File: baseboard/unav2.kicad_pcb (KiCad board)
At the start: 2 copper layers, 39 parts, among them IC1 MPM36xx, P1 SWD_TC, SW1 KEY_UP, SW2 KEY1, SW3 KEY0, SW4 Reset, U1 STM32F405RGTx, U2 AP2121AK-3.3

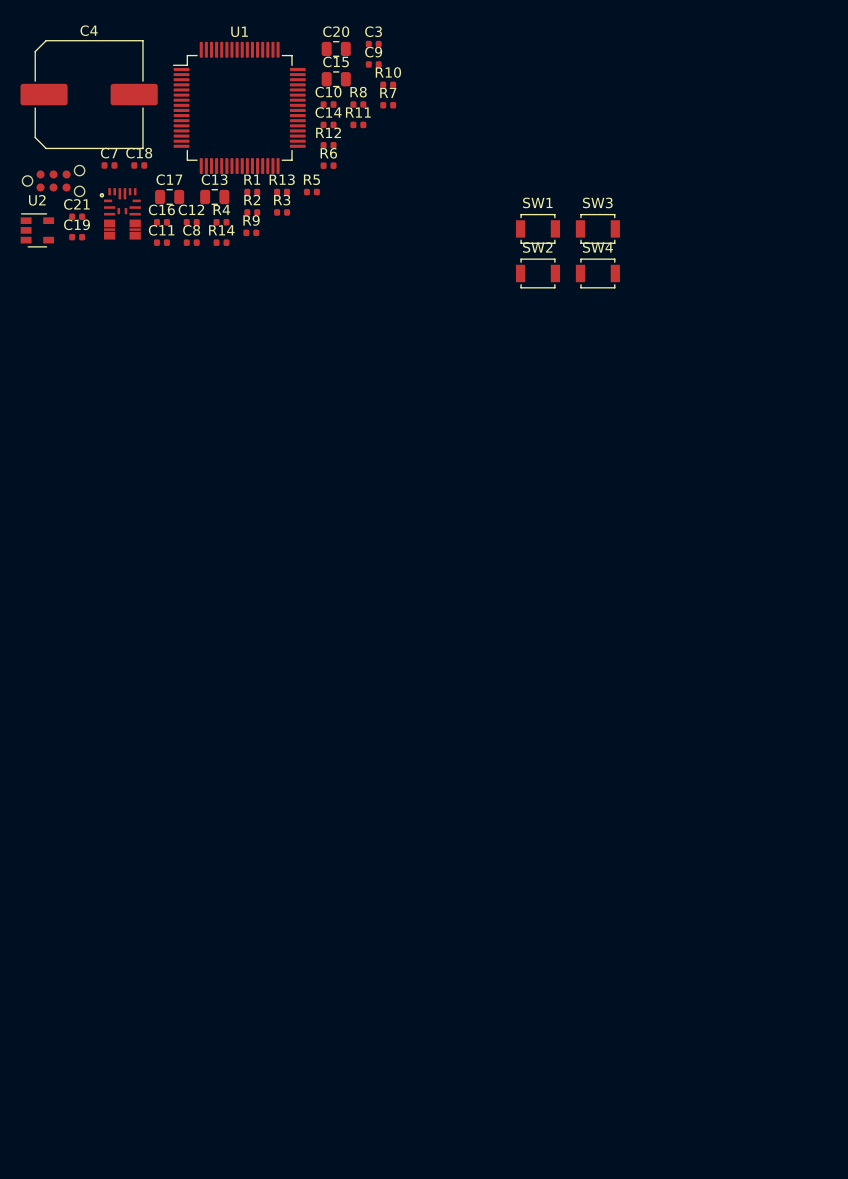
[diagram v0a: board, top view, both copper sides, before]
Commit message: test design of mcu+driver boards(do not build!! it is just less than an idea right now)
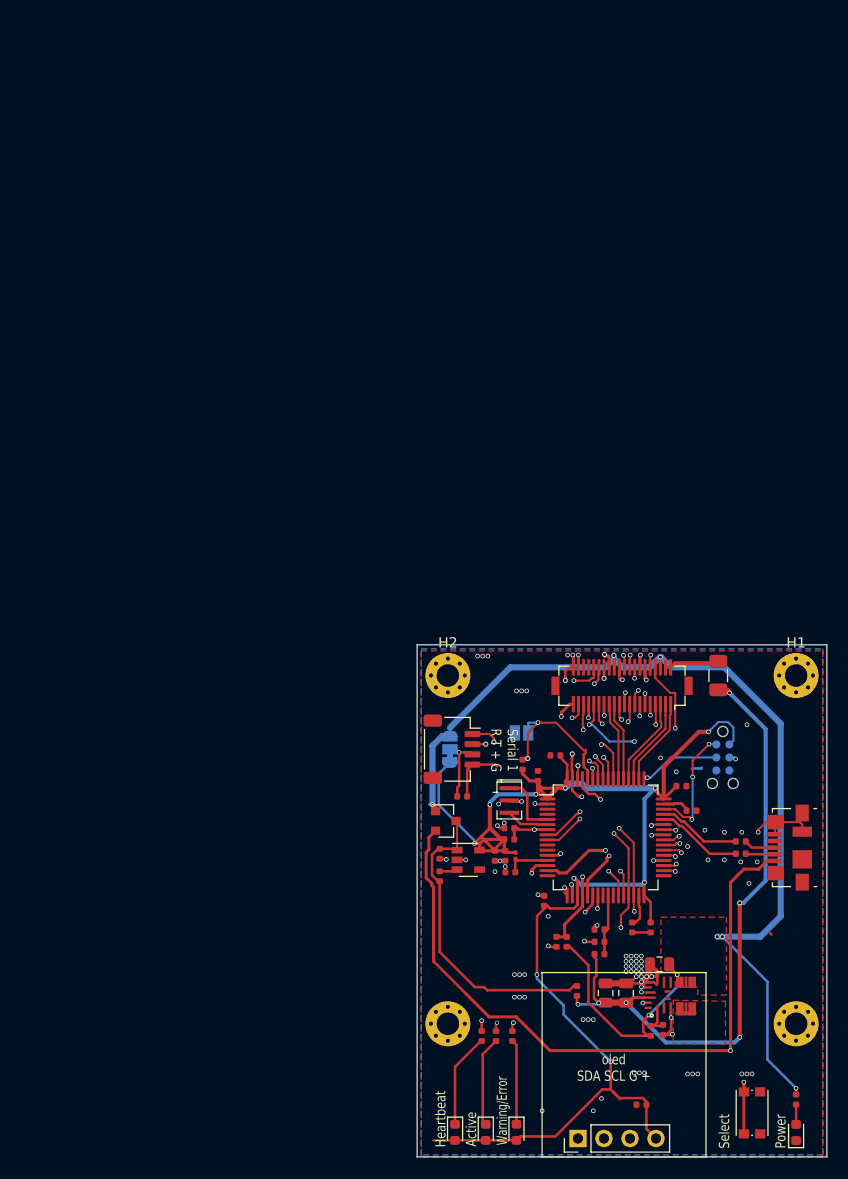
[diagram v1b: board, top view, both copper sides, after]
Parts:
- removed C20: 4.7uF, Capacitor_SMD:C_0805_2012Metric
- removed R11, R13: 10k, Resistor_SMD:R_0402_1005Metric
- removed R12, R8: 330, Resistor_SMD:R_0402_1005Metric
- removed R9: 22, Resistor_SMD:R_0402_1005Metric
- removed SW2: KEY1, Button_Switch_SMD:SW_SPST_B3U-1000P
- removed SW3: KEY0, Button_Switch_SMD:SW_SPST_B3U-1000P
- removed SW4: Reset, Button_Switch_SMD:SW_SPST_B3U-1000P
- added C22: C, Capacitor_SMD:C_0402_1005Metric, F.Cu at (154.4, 64.8)
- added C5: 100nF, Capacitor_SMD:C_0402_1005Metric, F.Cu at (167.8, 77.8)
- added C6: C, Capacitor_SMD:C_0402_1005Metric, F.Cu at (171.9, 94.9)
- added D1: White, LED_SMD:LED_0603_1608Metric, F.Cu at (187.0, 97.6)
- added D2: BAT54C, Package_TO_SOT_SMD:SOT-23, F.Cu at (152.8, 67.2)
- added D3: Blue, LED_SMD:LED_0603_1608Metric, F.Cu at (153.7, 97.6)
- added D4: Yellow, LED_SMD:LED_0603_1608Metric, F.Cu at (156.7, 97.6)
- added D5: Red, LED_SMD:LED_0603_1608Metric, F.Cu at (159.7, 97.6)
- added F1: Polyfuse_Small, Fuse:Fuse_1206_3216Metric, F.Cu at (179.4, 53.0)
- added H1: MountingHole, MountingHole:MountingHole_2.2mm_M2_Pad_Via, F.Cu at (187.0, 53.0)
- added H2: MountingHole, MountingHole:MountingHole_2.2mm_M2_Pad_Via, F.Cu at (153.0, 53.0)
- added H3: MountingHole, MountingHole:MountingHole_2.2mm_M2_Pad_Via, F.Cu at (153.0, 87.0)
- added H4: MountingHole, MountingHole:MountingHole_2.2mm_M2_Pad_Via, F.Cu at (187.0, 87.0)
- added J1: Conn_02x20_Top_Bottom, agg-kicad:Hirose_DF12_DF12B-40DS-0.5V(86), F.Cu at (170.0, 54.0)
- added J4: SERIAL1, Connector_JST:JST_SH_SM04B-SRSS-TB_1x04-1MP_P1.00mm_Horizontal, F.Cu at (153.4, 60.2)
- added J5: OLED, Connector_PinHeader_2.54mm:PinHeader_1x04_P2.54mm_Vertical, F.Cu at (165.7, 98.2)
- added J6: USB_B_Micro, Connector_USB:USB_Micro-B_Molex_47346-0001, F.Cu at (186.4, 69.8)
- added JP1: BOOT, Jumper:SolderJumper-2_P1.3mm_Open_Pad1.0x1.5mm, B.Cu at (160.2, 58.6)
- added JP3: S1_VSEL, Jumper:SolderJumper-3_P1.3mm_Bridged12_RoundedPad1.0x1.5mm, B.Cu at (153.2, 60.2)
- added L1: L_Small, Inductor_SMD:L_0201_0603Metric, F.Cu at (159.6, 70.6)
- added R15: 1k, Resistor_SMD:R_0402_1005Metric, F.Cu at (167.8, 79.0)
- added R16: 1k, Resistor_SMD:R_0402_1005Metric, F.Cu at (187.0, 94.4)
- added R17: 330, Resistor_SMD:R_0402_1005Metric, F.Cu at (156.3, 88.2)
- added R18: 330, Resistor_SMD:R_0402_1005Metric, F.Cu at (157.7, 88.2)
- added R19: 330, Resistor_SMD:R_0402_1005Metric, F.Cu at (159.3, 88.2)
- added Y1: 8MHz, Crystal:Resonator_SMD_muRata_CSTxExxV-3Pin_3.0x1.1mm, F.Cu at (159.0, 65.2)
- added e: 22, Resistor_SMD:R_0402_1005Metric, F.Cu at (181.6, 69.2)
- C13: value 4.7uf -> 1uF; footprint Capacitor_SMD:C_0805_2012Metric -> Capacitor_SMD:C_0402_1005Metric
- C18: value 10nF -> 100nF
- C19: value 10nF -> 4.7uf; footprint Capacitor_SMD:C_0402_1005Metric -> Capacitor_SMD:C_0805_2012Metric
- C4: value SUPERCAP -> 100nF; footprint Capacitor_SMD:C_Elec_10x10.2 -> Capacitor_SMD:C_0402_1005Metric
- IC1: footprint agg:QFN-20-MPS-3x5x1.6mm -> agg-kicad:QFN-20-MPS-3x5x1.6mm
- P1: footprint agg:TC2030-NL -> Connector:Tag-Connect_TC2030-IDC-NL_2x03_P1.27mm_Vertical; moved to B.Cu
- R1: value 10 -> 49k
- R14: value 47K -> 47k
- R6: value 10K -> 22K
- R7: value 10K -> 47k
- SW1: footprint Button_Switch_SMD:SW_SPST_B3U-1000P -> Button_Switch_SMD:SW_Push_1P1T_NO_CK_KMR2
- moved C15 93.6 mm to (170.4, 84.0), turned to 90 degrees
- moved IC1 93.1 mm to (175.0, 84.2), turned to 90 degrees
- moved C4 90.4 mm to (162.4, 75.0), turned to 270 degrees
- moved C19 90.0 mm to (168.4, 84.0), turned to 90 degrees
- moved C3 89.9 mm to (171.0, 77.6), turned to 270 degrees
- moved R4 89.4 mm to (172.8, 87.7), turned to 270 degrees
- moved C17 88.9 mm to (173.7, 81.2), turned to 180 degrees
- moved SW1 88.8 mm to (182.7, 95.7), turned to 90 degrees
- moved R5 88.7 mm to (174.0, 87.6), turned to 90 degrees
- moved P1 86.2 mm to (179.8, 61.0), turned to 270 degrees
- moved C18 86.0 mm to (163.6, 79.0), turned to 270 degrees
- moved C7 84.8 mm to (176.8, 66.2)
- moved R10 82.6 mm to (181.6, 70.4)
- moved R2 82.4 mm to (165.6, 83.8), turned to 270 degrees
- moved C11 82.1 mm to (172.8, 77.6), turned to 90 degrees
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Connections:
- net +3.3VA renamed Net-(C14-Pad1)
- net /I_ABORT renamed /I_FAULT
- net /O_REG_ENABLE renamed /O_REG_EN
- net /PA11 renamed /USB_OTG_FS_DM
- net /PA13 renamed /SWDIO
- net /PA14 renamed /SWCK
- C10 pad 2: /+3.3_Standby -> +3V3
- C11 pad 2: /+3.3_Standby -> +3V3
- C12 pad 2: /+3.3_Standby -> +3V3
- C13 pad 2: /+3.3_Standby -> +3V3
- C14 pad 2: GNDA -> GND
- C17 pad 1: /+5V_EXT -> +5V
- C19 pad 1: /+5VDD -> /V_BATT
- C21 pad 1: GND -> /NRST
- C21 pad 2: /NRST -> GND
- C4 pad 2: /VBATT -> +3V3
- C8 pad 2: /+3.3_Standby -> +3V3
- C9 pad 2: /+3.3_Standby -> +3V3
- IC1 pad 11: Net-(IC1-Pad11) -> (no net)
- IC1 pad 18: Net-(IC1-Pad18) -> (no net)
- IC1 pad 2: Net-(IC1-Pad2) -> (no net)
- IC1 pad 7: /+5V_EXT -> +5V
- IC1 pad 8: /+5V_EXT -> +5V
- IC1 pad 9: /+5V_EXT -> +5V
- P1 pad 1: /+3.3_Standby -> +3V3
- P1 pad 6: Net-(P1-Pad6) -> (no net)
- R1 pad 1: Net-(D1-Pad2) -> /ADC_BATT_VOL
- R1 pad 2: /+3.3_Standby -> /V_BATT
- R14 pad 1: /+3.3_Standby -> +3V3
- R4 pad 2: /+5V_EXT -> +5V
- R6 pad 2: /+3.3_Standby -> +5V
- R7 pad 1: /BOOT0 -> +3V3
- R7 pad 2: /+3.3_Standby -> /BOOT0
- U1 pad 1: /VBATT -> +3V3
- U1 pad 10: /KEY1 -> (no net)
- U1 pad 11: /ADC_SPARE1 -> (no net)
- U1 pad 12: GNDA -> GND
- U1 pad 15: /PA1 -> /TIM_ENC2_B
- U1 pad 16: /ADC_TEMP -> (no net)
- U1 pad 17: /ADC1_IN3 -> /SPARE_1
- U1 pad 19: /+3.3_Standby -> +3V3
- U1 pad 2: /KEY0 -> /O_LED1
- U1 pad 21: /PA5 -> /TIM_ENC2_A
- U1 pad 22: /O_LED1 -> /O_LED2
- U1 pad 23: /O_LED2 -> /O_LED3
- U1 pad 24: /ADC_BATT_CUR -> (no net)
- U1 pad 26: /PB0 -> (no net)
- U1 pad 27: /PB1 -> /TIM_FAN_PWM
- U1 pad 3: Net-(C1-Pad2) -> (no net)
- U1 pad 32: /+3.3_Standby -> +3V3
- U1 pad 33: /I2C_SMBA -> (no net)
- U1 pad 35: /PB14 -> /TIM_MOT1_B
- U1 pad 36: /PB15 -> /TIM_MOT2_B
- U1 pad 38: /PC7 -> /TIM_MOT1_A
- U1 pad 39: /PC8 -> /TIM_MOT2_A
- U1 pad 4: Net-(C2-Pad2) -> (no net)
- U1 pad 41: /PA8 -> /TIM_ENC1_A
- U1 pad 42: /PA9 -> /TIM_ENC1_B
- U1 pad 43: /O_PWR_MAIN_EN -> /O_PWR_MOT_EN
- U1 pad 45: /PA12 -> /USB_OTG_FS_DP
- U1 pad 48: /+3.3_Standby -> +3V3
- U1 pad 53: /PC12 -> /SER2_TX
- U1 pad 54: /PD2 -> /SER2_RX
- U1 pad 55: /PB3 -> /SPI1_SCK
- U1 pad 56: /PB4 -> /SPI1_MISO
- U1 pad 57: /PB5 -> /SPI1_MOSI
- U1 pad 58: /PB6 -> /SER1_TX
- U1 pad 59: /PB7 -> /SER1_RX
- U1 pad 64: /+3.3_Standby -> +3V3
- U2 pad 4: Net-(U2-Pad4) -> (no net)
- U2 pad 5: /+3.3_Standby -> +3V3
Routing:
- net +3V3: track 0.00 -> 152.7 mm, vias 0 -> 10
- net +5V: track 0.00 -> 122.0 mm, vias 0 -> 8
- net /5V_USB: track 0.00 -> 67.7 mm, vias 0 -> 1
- net /V_BATT: track 0.00 -> 63.3 mm, vias 0 -> 6
- net GND: track 0.00 -> 57.4 mm, vias 0 -> 88
- net /I2C_SDA: track 0.00 -> 50.4 mm, vias 0 -> 3
- net /I2C_SCL: track 0.00 -> 48.5 mm, vias 0 -> 3
- net /NRST: track 0.00 -> 39.5 mm, vias 0 -> 2
- net /I_KEY_UP: track 0.00 -> 39.3 mm, vias 0 -> 2
- net /TIM_ENC2_B: track 0.00 -> 31.8 mm, vias 0 -> 2
- net Net-(C16-Pad1): track 0.00 -> 30.6 mm
- net /SPARE_1: track 0.00 -> 29.2 mm, vias 0 -> 2
- net /TIM_ENC2_A: track 0.00 -> 28.1 mm, vias 0 -> 2
- net /I_FAN_INDEX: track 0.00 -> 28.1 mm, vias 0 -> 2
- net /TIM_FAN_PWM: track 0.00 -> 26.7 mm, vias 0 -> 2
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- added copper zone on F.Cu, net +5V
- added copper zone on B.Cu, net GND
- added copper zone on F.Cu, net GND
- added copper zone on F.Cu, net Net-(IC1-Pad4)
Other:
- board outline added: 40 x 50 mm
- copper layers 2 -> 4
- net class Default: via_dia 0.8 -> 0.5; via_drill 0.4 -> 0.3
- net class VBATT added: clearance 0.3, trace_width 0.25, via_dia 0.5, via_drill 0.3
- board text added: "Active"
- board text added: "Heartbeat"
- board text added: "Power"
- board text added: "Select"
- board text added: "Serial 1 R T + G"
- board text added: "Warning/Error"
- board text added: "oled SDA SCL G +"
